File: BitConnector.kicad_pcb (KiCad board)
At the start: 2 copper layers, 21.1 x 53.3 mm, 16 parts, among them J1 JTAG, SW1 reset, U1 XC95##XL-VQ44

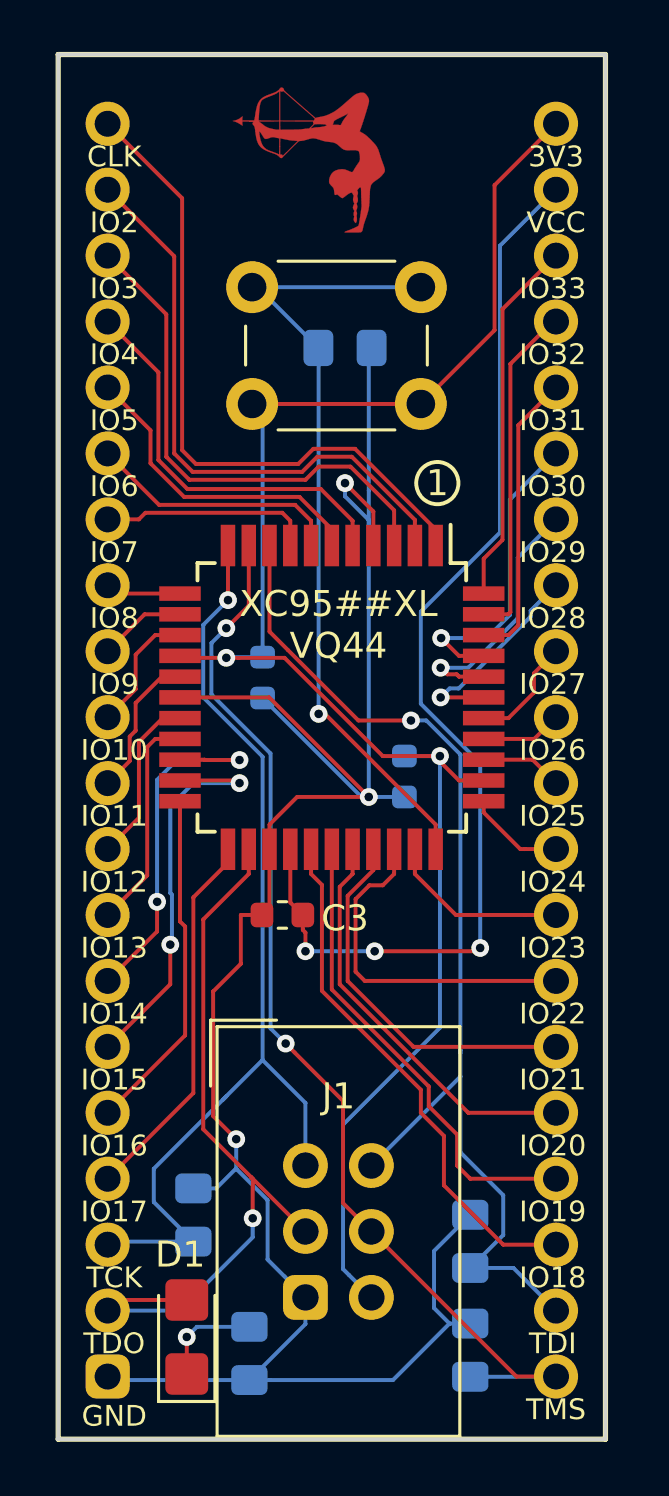
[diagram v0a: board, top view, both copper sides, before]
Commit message: Introduce BitConnector_v4X     - Add hardware debouncing via schmitt trigger action     - The Schmnitt Triger adds another external inverter. Usable over J2.     - As an alternative, add jumper to bridge the Schmitt trigger.         Use this if the component is not available.     - Partial redesign of the routing     - Add schematic as PDF now
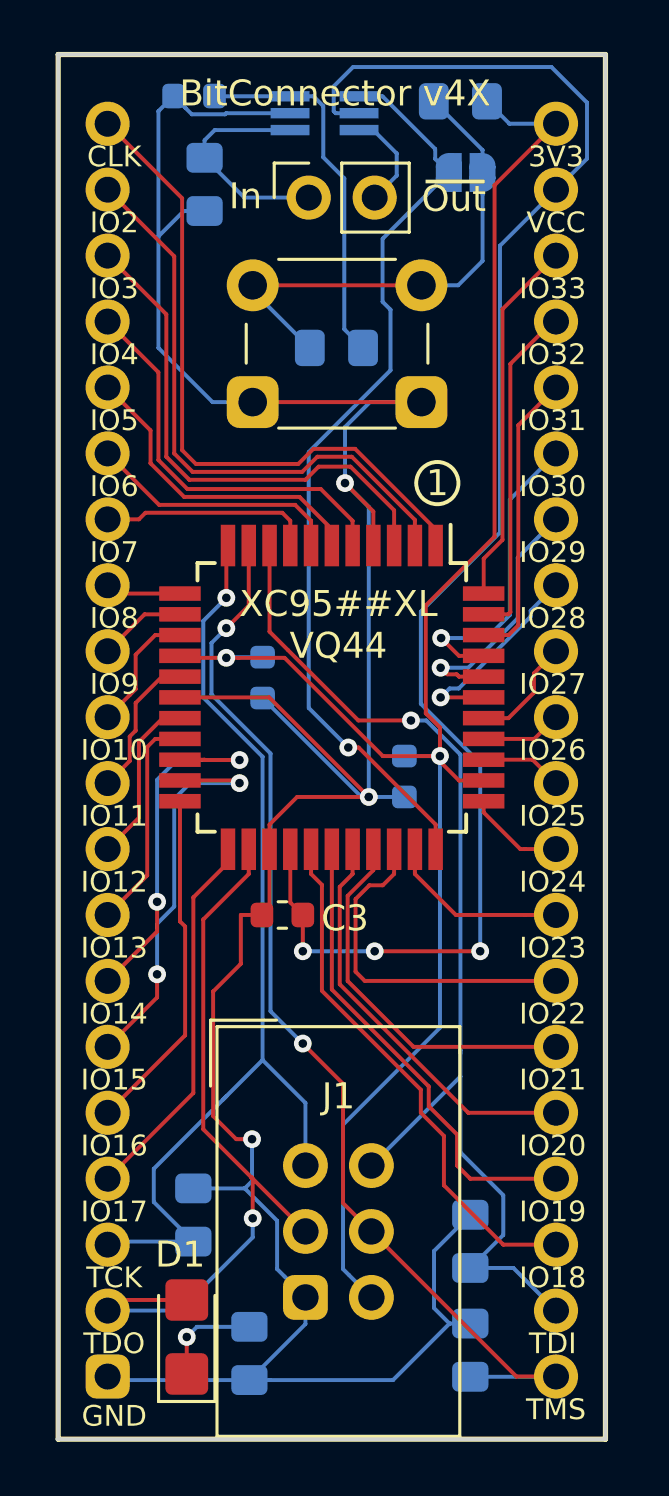
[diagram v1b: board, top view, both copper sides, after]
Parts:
- removed G1: JandM-LOGO, CPLD_DIP_Projekt:logo_f.Mask
- removed G1: JandM-LOGO, CPLD_DIP_Projekt:logo
- added C4: 100nF, Capacitor_SMD:C_0603_1608Metric, B.Cu at (164.5, 73.4)
- added G***: LOGO, eigene Lib:logo, B.Cu at (171.4, 106.5)
- added J2: Conn_01x02, Connector_PinSocket_2.54mm:PinSocket_1x02_P2.54mm_Vertical, F.Cu at (168.9, 77.3)
- added JP1: disable_schmitt_trigger_action, Jumper:SolderJumper-2_P1.3mm_Open_RoundedPad1.0x1.5mm, B.Cu at (175.0, 76.3)
- added R6: 10K, Resistor_SMD:R_0805_2012Metric_Pad1.15x1.40mm_HandSolder, B.Cu at (174.8, 73.6)
- added R7: 10K, Resistor_SMD:R_0805_2012Metric_Pad1.15x1.40mm_HandSolder, B.Cu at (164.9, 76.8)
- added U2: 74LVC2G14, Package_TO_SOT_SMD:SOT-363_SC-70-6_Handsoldering, B.Cu at (169.5, 74.0)
- R1, R2, R3: value 4K7 -> 10K
- R5: value 4K7 -> 100K
- moved SW1 7.93 mm to (166.8, 80.6), turned to 0 degrees
- moved R5 0.33 mm to (170.0, 83.1)
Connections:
- R5 pad 1: Net-(R5-Pad1) -> Net-(JP1-Pad2)
- R5 pad 2: GND -> Net-(C4-Pad1)
- SW1 pad 1: +3V3 -> Net-(JP1-Pad2)
- SW1 pad 2: Net-(R5-Pad1) -> GND
- U1 pad 33: Net-(R5-Pad1) -> Net-(JP1-Pad1)
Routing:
- net Net-(JP1-Pad1): track 0.00 -> 35.7 mm, vias 0 -> 1
- net Net-(R5-Pad1): track 31.4 -> 0.00 mm, vias 1 -> 0
- net GND: track 89.8 -> 117.5 mm
- net Net-(JP1-Pad2): track 0.00 -> 19.6 mm
- net VCC: track 43.3 -> 59.9 mm
- net Net-(C4-Pad1): track 0.00 -> 14.4 mm
- net Net-(J2-Pad1): track 0.00 -> 8.78 mm
- net Net-(J2-Pad2): track 0.00 -> 3.88 mm
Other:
- board text added: "BitConnector v4X"
- board text added: "In"
- board text added: "Out"
- board text added: "_"
- board text removed: "BitConnector v3X"

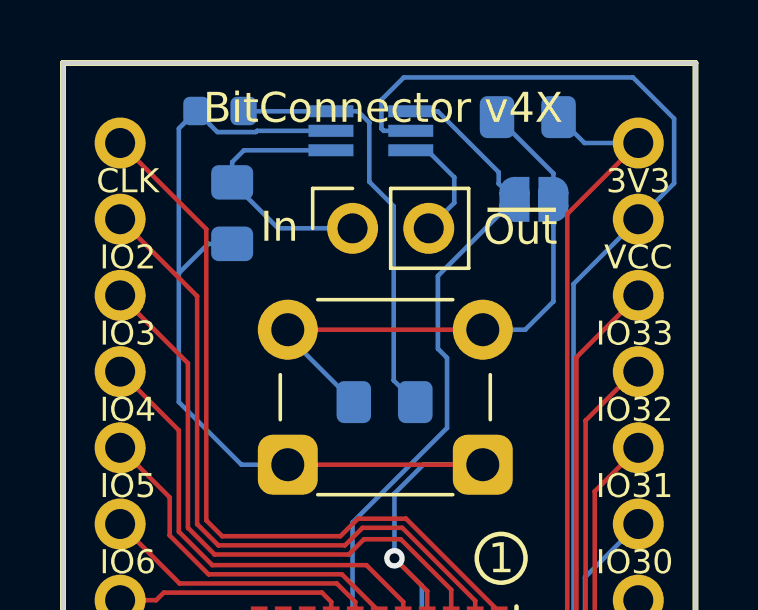
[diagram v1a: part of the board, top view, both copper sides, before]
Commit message: Change package for 74LVC2G14 from SOT363 to SOT457
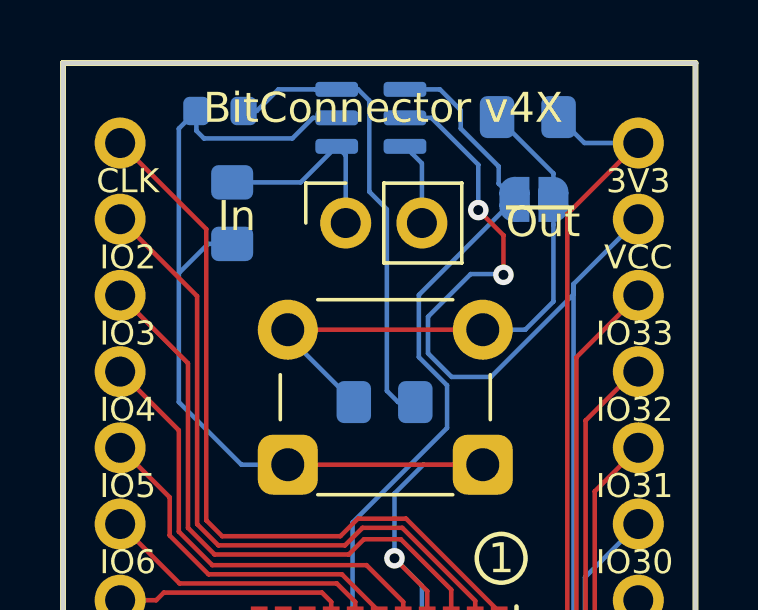
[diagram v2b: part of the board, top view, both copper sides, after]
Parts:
- U2: footprint Package_TO_SOT_SMD:SOT-363_SC-70-6_Handsoldering -> Package_SO:SC-74-6_1.5x2.9mm_P0.95mm
- moved U2 0.43 mm to (169.5, 73.6)
- moved J2 0.29 mm to (168.7, 77.1)
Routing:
- net Net-(J2-Pad1): track 8.78 -> 6.66 mm
- net VCC: track 59.9 -> 61.6 mm, vias 3 -> 5
- net Net-(JP1-Pad1): track 35.7 -> 37.2 mm
- net Net-(C4-Pad1): track 14.4 -> 15.7 mm
- net Net-(J2-Pad2): track 3.88 -> 2.79 mm
- net GND: track 117.5 -> 118.5 mm

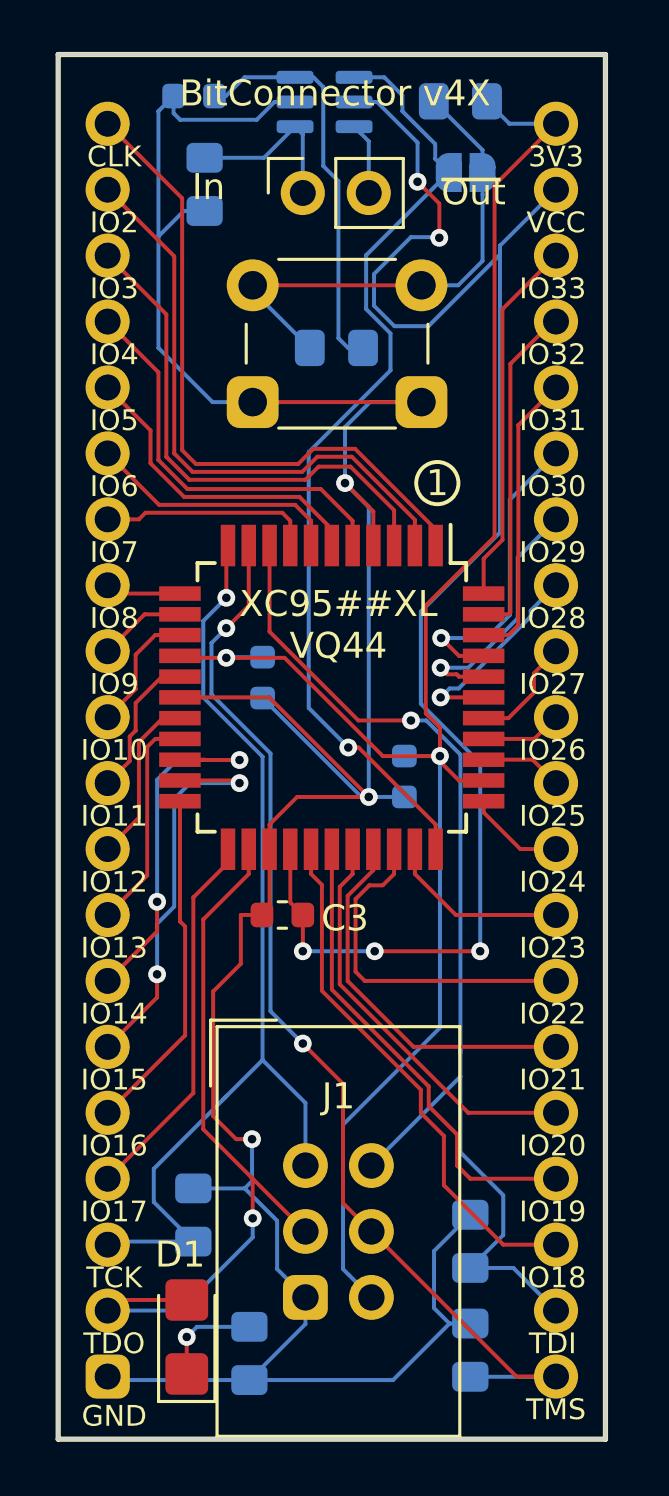
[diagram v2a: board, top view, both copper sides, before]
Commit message: first attempt of the new v5X version
    details:
    	- switch solder pad for resistors from 1.15mm to 1.20mm
	- add additional 10nF bypass capacitor according to
	  Xilinx XAPP104 (3.0.1) specification
	- Completely new board layout created to improve
	  GND and Vcc connection and suppress interference signals
	- fallback to v3X (minimal configuration) is retained
	- 74LVC2G14 (schmitt trigger) now has a better footprint
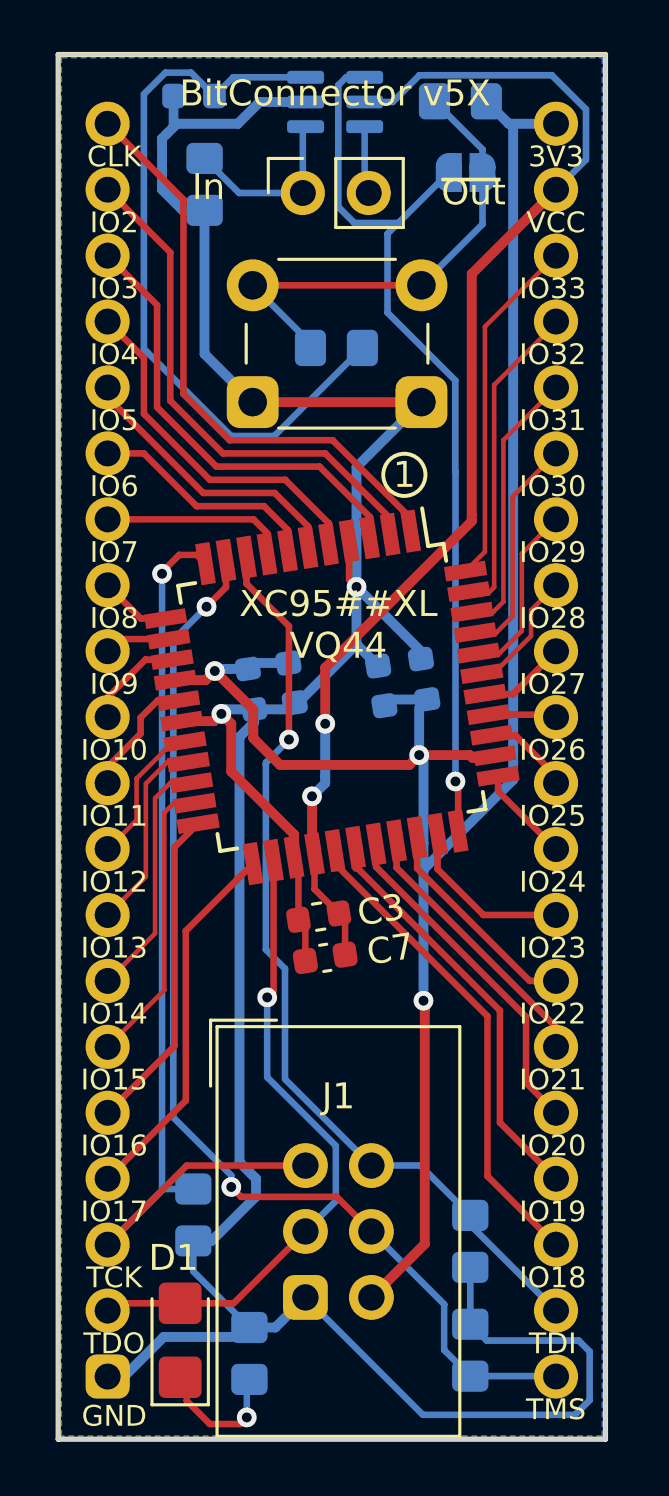
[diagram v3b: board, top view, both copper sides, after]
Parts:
- removed G***: LOGO, eigene Lib:logo
- added C5: 10nF, Capacitor_SMD:C_0603_1608Metric, B.Cu at (168.2, 96.0)
- added C6: 10nF, Capacitor_SMD:C_0603_1608Metric, B.Cu at (171.7, 96.1)
- added C7: 10nF, Capacitor_SMD:C_0603_1608Metric, F.Cu at (169.5, 106.6)
- R1, R2, R3, R4, R5, R6, R7: footprint Resistor_SMD:R_0805_2012Metric_Pad1.15x1.40mm_HandSolder -> Resistor_SMD:R_0805_2012Metric_Pad1.20x1.40mm_HandSolder
- moved C2 3.82 mm to (173.4, 95.8), turned to 279 degrees
- moved C3 1.40 mm to (169.3, 105.0), turned to 9 degrees
- moved C1 0.63 mm to (166.7, 96.2), turned to 279 degrees
- moved U2 0.41 mm to (169.9, 73.6)
- moved D1 0.28 mm to (164.0, 121.3)
- turned R1 to 270 degrees
- turned R3 to 90 degrees
- turned R4 to 270 degrees
- turned U1 to 279 degrees
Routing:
- net VCC: track 61.6 -> 47.0 mm, vias 5 -> 2
- net Net-(C4-Pad1): track 15.7 -> 28.3 mm
- net +3V3: track 69.1 -> 77.2 mm, vias 2 -> 3
- net /JTAG_TDI: track 43.2 -> 36.6 mm
- net /GP_IO_22: track 13.5 -> 8.33 mm
- net /GP_IO_14: track 14.3 -> 9.45 mm, vias 2 -> 0
- net GND: track 118.5 -> 123.0 mm, vias 3 -> 2
- net /GP_IO_15: track 15.7 -> 11.3 mm, vias 2 -> 0
- net /JTAG_TDO: track 30.0 -> 25.6 mm
- net /GP_IO_21: track 14.6 -> 10.5 mm
- net /GP_IO_30: track 11.9 -> 8.66 mm, vias 1 -> 0
- net /GP_IO_28: track 8.03 -> 4.85 mm, vias 1 -> 0
- net /GP_IO_29: track 9.98 -> 6.86 mm, vias 1 -> 0
- net /CLK_GP_IO_1: track 25.9 -> 22.9 mm
- net /GP_IO_2: track 23.0 -> 20.1 mm
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- added copper zone on B.Cu, net GND
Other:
- net class Default: clearance 0.1524 -> 0.1778; trace_width 0.1524 -> 0.1778; via_dia 0.6858 -> 0.762; via_drill 0.33 -> 0.381
- rule trace_clearance: 0.1524 -> 0.1778
- board text added: "BitConnector v5X"
- board text added: "by Micha @2021"
- board text removed: "BitConnector v4X"
- board text removed: "by MiJA @2019"

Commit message: Revise board layout
according to suggestions for improvement, see under:
https://www.mikrocontroller.net/topic/492067
thx Lothar
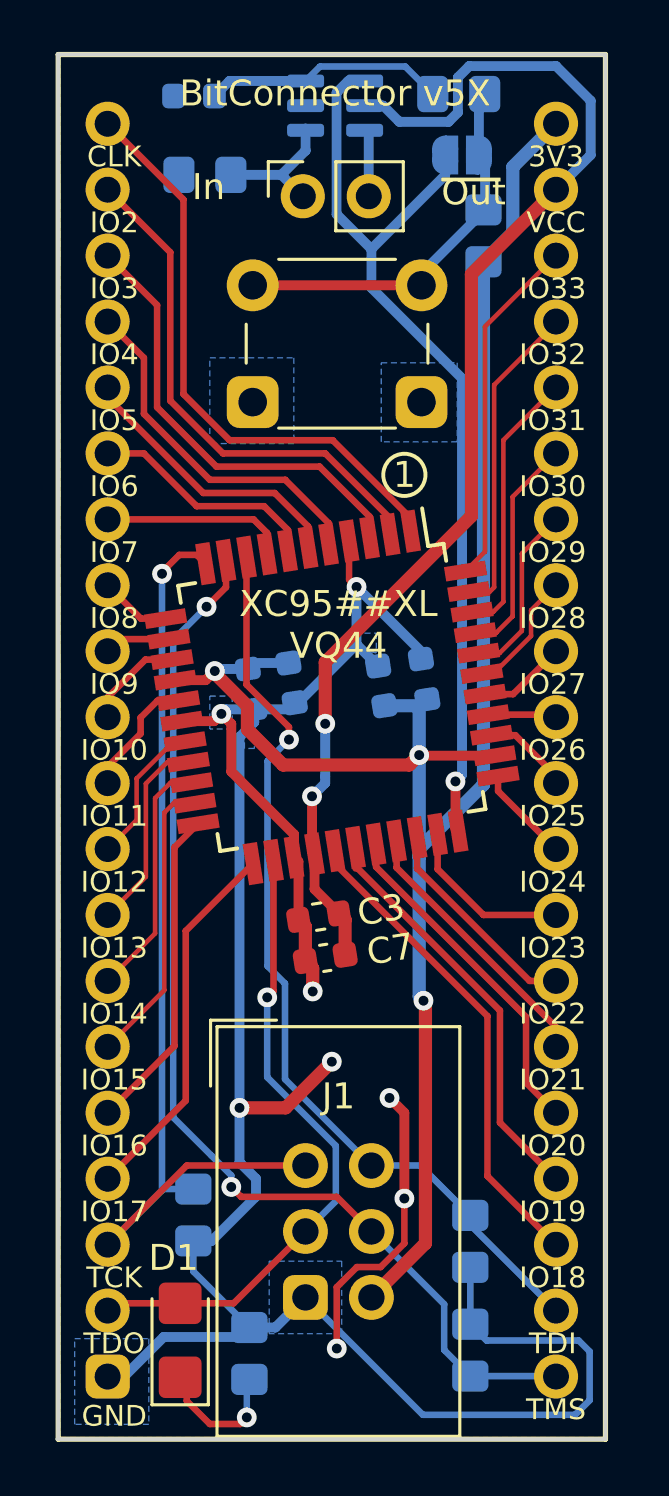
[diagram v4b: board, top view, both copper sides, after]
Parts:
- moved R5 10.9 mm to (174.7, 73.3), turned to 180 degrees
- moved R6 5.26 mm to (175.6, 78.7), turned to 90 degrees
- moved J1 0.69 mm to (174.8, 75.6)
- moved R7 0.37 mm to (164.9, 76.4), turned to 180 degrees
- moved U2 0.14 mm to (169.9, 73.7)
- moved J2 0.13 mm to (168.7, 77.2)
- renumbered JP1 to J1
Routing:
- net Net-(C4-Pad1): track 28.3 -> 9.32 mm
- net GND: track 123.0 -> 105.7 mm, vias 2 -> 8
- net Net-(JP1-Pad2): track 18.7 -> 15.2 mm
- net VCC: track 47.0 -> 49.1 mm
- net Net-(J2-Pad1): track 6.94 -> 5.55 mm
- net Net-(JP1-Pad1): track 35.9 -> 37.2 mm
- net +3V3: track 77.2 -> 76.5 mm

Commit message: Adjust README and graphics to the new version 5
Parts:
- added G***: LOGO, logo:tux_logo, B.Cu at (169.4, 103.2)
